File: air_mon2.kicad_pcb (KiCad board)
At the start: 2 copper layers, 95 x 60 mm, 16 parts, among them J1 Conn_01x19, J2 Conn_01x19, J3 Barrel_Jack_Switch, U1 nodemcu-32s, U2 PMS7003, U3 WZ-H3, U4 WZ-H3-K, U5 TW-SGP30

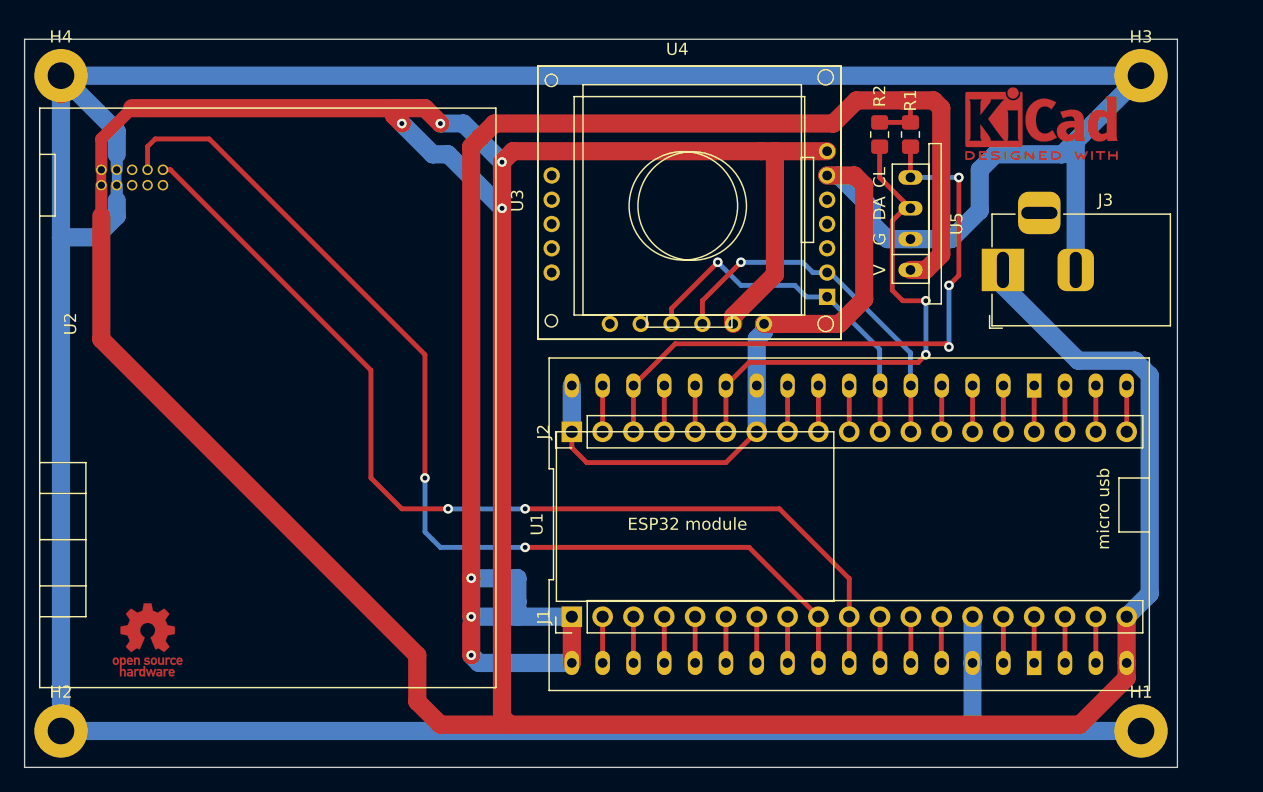
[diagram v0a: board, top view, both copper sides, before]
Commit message: update, v1.1
1. add sth31
2. fix wz-h3
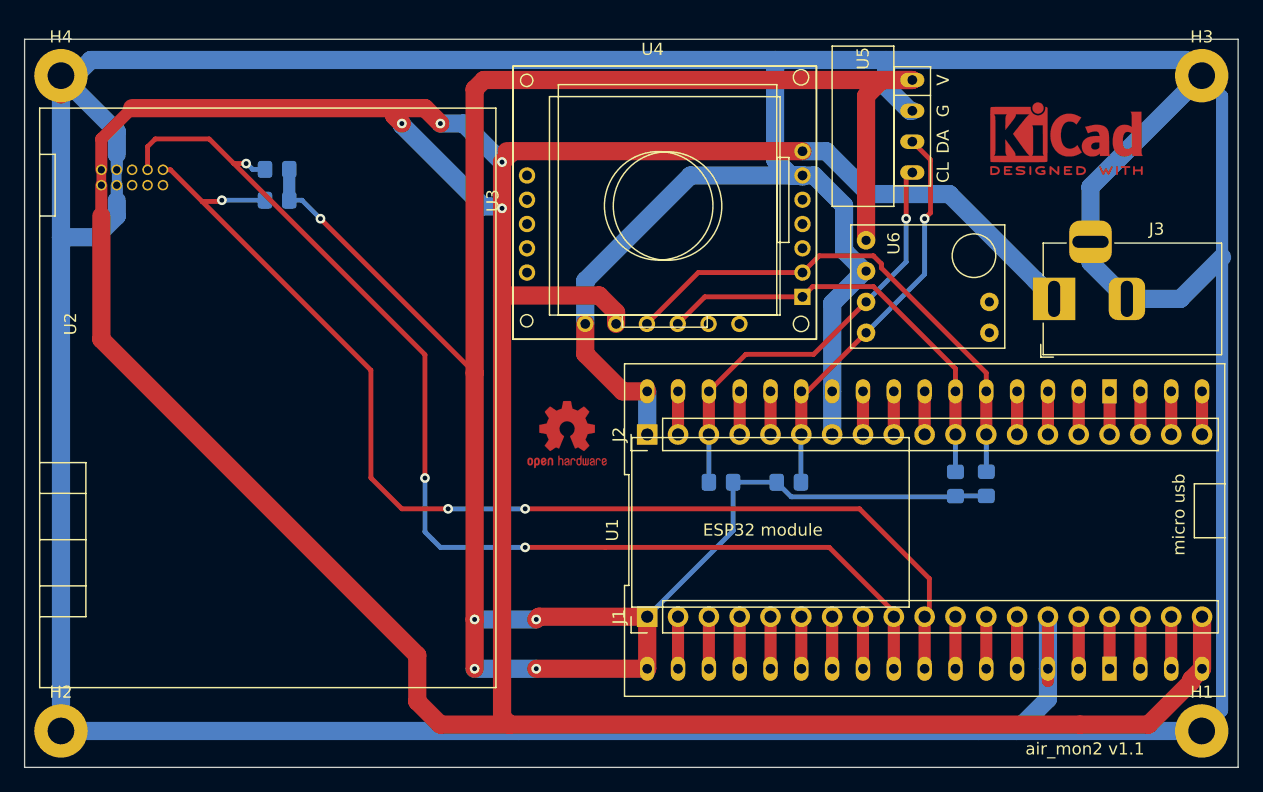
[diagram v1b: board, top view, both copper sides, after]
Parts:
- removed the REF** at (89.5, 107.6)
- added R3: 10K, Resistor_SMD:R_0805_2012Metric_Pad1.20x1.40mm_HandSolder, B.Cu at (100.2, 68.8)
- added R4: 10K, Resistor_SMD:R_0805_2012Metric_Pad1.20x1.40mm_HandSolder, B.Cu at (100.2, 71.4)
- added R5: 10K, Resistor_SMD:R_0805_2012Metric_Pad1.20x1.40mm_HandSolder, B.Cu at (158.6, 94.7)
- added R6: 10K, Resistor_SMD:R_0805_2012Metric_Pad1.20x1.40mm_HandSolder, B.Cu at (156.1, 94.7)
- added REF**: OSHW-Logo2_7.3x6mm_Copper, Symbol:OSHW-Logo2_7.3x6mm_Copper, F.Cu at (124.1, 90.7)
- added U6: GY-SHT31-D, air_mon2:GY-SHT31-D, F.Cu at (147.4, 73.4)
- R1, R2: moved to B.Cu
- moved R1 32.6 mm to (136.8, 94.6), turned to 180 degrees
- moved R2 29.6 mm to (142.3, 94.6), turned to 0 degrees
- moved U5 8.03 mm to (152.5, 65.3), turned to 270 degrees
- moved U1 6.23 mm to (153.5, 98.5)
- moved J2 6.22 mm to (130.7, 90.7)
- moved J1 6.21 mm to (130.7, 105.7)
- moved H1 5.00 mm to (176.4, 115.1)
- moved H3 5.00 mm to (176.4, 61.1)
- moved J3 4.84 mm to (164.2, 79.5)
- moved REF** 2.40 mm to (165.2, 66.3)
- moved U3 2.03 mm to (144.6, 82.8)
- moved U4 2.03 mm to (144.6, 82.8)
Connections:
- J3 pad 3: Net-(J3-Pad3) -> GND
- U3 pad 1: Net-(U3-Pad1) -> GND
- U3 pad 2: Net-(U3-Pad2) -> +5V
- U3 pad 3: Net-(J2-Pad11) -> Net-(J2-Pad12)
- U3 pad 4: Net-(J2-Pad12) -> Net-(J2-Pad11)
- U3 pad 5: +5V -> Net-(U3-Pad5)
- U3 pad 6: GND -> Net-(U3-Pad6)
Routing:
- net GND: track 362.6 -> 446.9 mm
- net +3V3: track 129.2 -> 192.3 mm, vias 3 -> 5
- net Net-(J2-Pad3): track 52.2 -> 36.4 mm, vias 3 -> 1
- net Net-(J2-Pad12): track 30.0 -> 42.9 mm, vias 1 -> 0
- net Net-(J1-Pad10): track 82.7 -> 95.0 mm, vias 2 -> 3
- net Net-(J2-Pad6): track 43.4 -> 33.4 mm, vias 2 -> 1
- net Net-(J1-Pad9): track 86.2 -> 96.1 mm, vias 2 -> 3
- net +5V: track 298.2 -> 288.7 mm
- net Net-(J2-Pad11): track 29.8 -> 35.5 mm, vias 1 -> 0
- net Net-(J2-Pad2): track 3.81 -> 5.17 mm
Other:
- board size 95 x 60 mm -> 100 x 60 mm
- board text added: "air_mon2 v1.1"
